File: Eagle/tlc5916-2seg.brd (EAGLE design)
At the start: 98.7 x 48.2 mm, 8 parts, among them IC1 HD-A544D, U1 TLC5916IN, U2 TLC5916IN

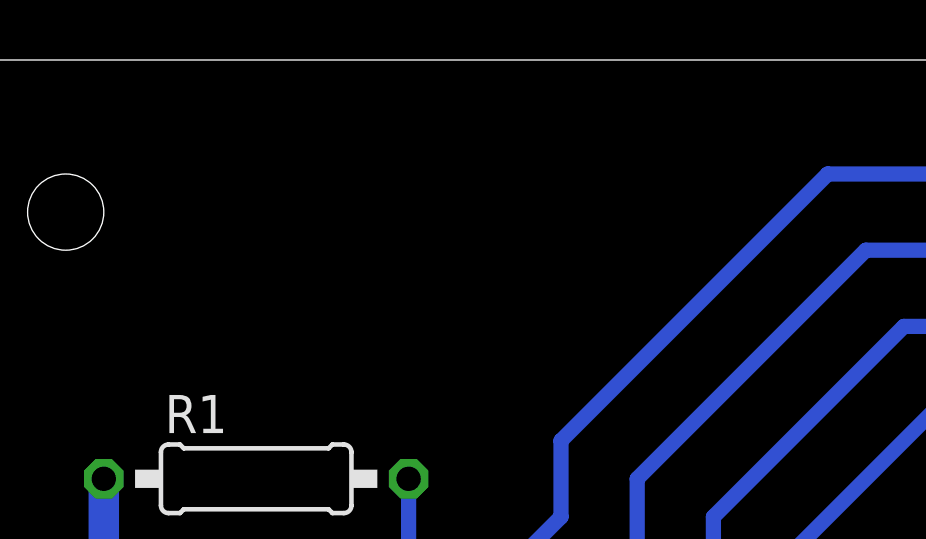
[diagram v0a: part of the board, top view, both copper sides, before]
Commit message: Fixed R1, R2 values, added revision number to PCB
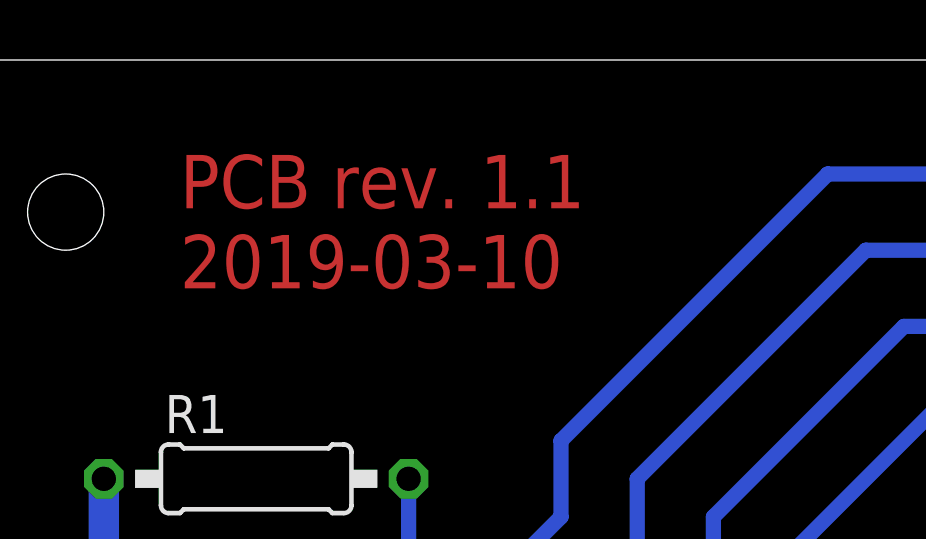
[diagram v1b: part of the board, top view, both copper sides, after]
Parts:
- R1, R2: value 5k -> 1k
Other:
- board text added: "PCB rev. 1.1 2019-03-10"
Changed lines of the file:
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@@
 <drawing>
 <settings>
-<setting alwaysvectorfont="no"/>
+<setting alwaysvectorfont="yes"/>
 <setting verticaltext="up"/>
 </settings>
@@
 <dimension x1="0" y1="49.53" x2="99.06" y2="49.53" x3="49.53" y3="50.8" textsize="1.778" layer="1"/>
 <dimension x1="-1.27" y1="48.26" x2="-1.27" y2="0" x3="-2.54" y3="24.13" textsize="1.778" layer="1"/>
+<text x="8.89" y="40.64" size="1.778" layer="1">PCB rev. 1.1
+2019-03-10</text>
 </plain>
 <attributes>
@@
 <attribute name="VALUE" x="45.085" y="12.065" size="1.778" layer="27"/>
 </element>
-<element name="R1" library="rcl" library_urn="urn:adsk.eagle:library:334" package="0207/10" package3d_urn="urn:adsk.eagle:package:23491/1" value="5k" x="11.43" y="34.29" smashed="yes">
+<element name="R1" library="rcl" library_urn="urn:adsk.eagle:library:334" package="0207/10" package3d_urn="urn:adsk.eagle:package:23491/1" value="1k" x="11.43" y="34.29" smashed="yes">
 <attribute name="NAME" x="8.382" y="35.814" size="1.27" layer="25" ratio="10"/>
 <attribute name="SPICEPREFIX" value="R" x="30.48" y="-22.86" size="1.778" layer="27" display="off"/>
 <attribute name="VALUE" x="9.1694" y="33.655" size="1.27" layer="27" ratio="10"/>
 </element>
-<element name="R2" library="rcl" library_urn="urn:adsk.eagle:library:334" package="0207/10" package3d_urn="urn:adsk.eagle:package:23491/1" value="5k" x="88.9" y="15.24" smashed="yes" rot="R180">
+<element name="R2" library="rcl" library_urn="urn:adsk.eagle:library:334" package="0207/10" package3d_urn="urn:adsk.eagle:package:23491/1" value="1k" x="88.9" y="15.24" smashed="yes" rot="R180">
 <attribute name="NAME" x="91.948" y="13.716" size="1.27" layer="25" ratio="10" rot="R180"/>
 <attribute name="SPICEPREFIX" value="R" x="57.15" y="72.39" size="1.778" layer="27" rot="R180" display="off"/>
@@
 </drawing>
 <compatibility>
+<note version="6.3" minversion="6.2.2" severity="warning">
+Since Version 6.2.2 text objects can contain more than one line,
+which will not be processed correctly with this version.
+</note>
 <note version="8.2" severity="warning">
 Since Version 8.2, EAGLE supports online libraries. The ids
